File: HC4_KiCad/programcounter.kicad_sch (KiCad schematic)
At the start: 20 parts, among them IC13 74HC161, IC14 74HC161, IC15 74HC161

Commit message: フットプリントをSOPに変更
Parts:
- CP12, CP13, CP14: footprint Capacitor_THT:C_Disc_D3.0mm_W1.6mm_P2.50mm -> Capacitor_SMD:C_0603_1608Metric
- IC13, IC14, IC15: footprint Package_DIP:DIP-16_W7.62mm_Socket -> Package_SO:SO-16_5.3x10.2mm_P1.27mm
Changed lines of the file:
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@@
 			)
 		)
-		(property "Footprint" "Package_DIP:DIP-16_W7.62mm_Socket"
+		(property "Footprint" "Package_SO:SO-16_5.3x10.2mm_P1.27mm"
 			(at 127 33.02 0)
 			(effects
@@
 			)
 		)
-		(property "Footprint" "Capacitor_THT:C_Disc_D3.0mm_W1.6mm_P2.50mm"
+		(property "Footprint" "Capacitor_SMD:C_0603_1608Metric"
 			(at 125.4252 182.88 0)
 			(effects
@@
 			)
 		)
-		(property "Footprint" "Capacitor_THT:C_Disc_D3.0mm_W1.6mm_P2.50mm"
+		(property "Footprint" "Capacitor_SMD:C_0603_1608Metric"
 			(at 131.7752 182.88 0)
 			(effects
@@
 			)
 		)
-		(property "Footprint" "Package_DIP:DIP-16_W7.62mm_Socket"
+		(property "Footprint" "Package_SO:SO-16_5.3x10.2mm_P1.27mm"
 			(at 127 76.2 0)
 			(effects
@@
 			)
 		)
-		(property "Footprint" "Package_DIP:DIP-16_W7.62mm_Socket"
+		(property "Footprint" "Package_SO:SO-16_5.3x10.2mm_P1.27mm"
 			(at 127 120.65 0)
 			(effects
@@
 			)
 		)
-		(property "Footprint" "Capacitor_THT:C_Disc_D3.0mm_W1.6mm_P2.50mm"
+		(property "Footprint" "Capacitor_SMD:C_0603_1608Metric"
 			(at 119.0752 182.88 0)
 			(effects

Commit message: 基板ぬ
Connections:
- net at LD30.1 (K): now also RN5.2 (R1.2); no longer RN5.5 (R4.2)
- net at RN5.3 (R2.2): now also LD27.1 (K); no longer LD24.1 (K)
- net at LD29.1 (K): now also RN4.6 (R5.2); no longer RN4.9 (R8.2)
- net at RN5.4 (R3.2): now also LD24.1 (K); no longer LD27.1 (K)
- net at RN5.7 (R6.2): now also LD28.1 (K); no longer LD25.1 (K)
- net at LD20.1 (K): now also RN4.9 (R8.2); no longer RN4.6 (R5.2)
- net at RN5.8 (R7.2): now also LD25.1 (K); no longer LD28.1 (K)
- net at LD21.1 (K): now also RN5.5 (R4.2); no longer RN5.2 (R1.2)
- net at RN5.9 (R8.2): now also LD22.1 (K); no longer LD31.1 (K)
- net at LD23.1 (K): now also RN4.8 (R7.2); no longer RN4.7 (R6.2)
- net at RN5.6 (R5.2): now also LD31.1 (K); no longer LD22.1 (K)
- net at LD26.1 (K): now also RN4.7 (R6.2); no longer RN4.8 (R7.2)
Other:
- moved on the sheet: RN4E, RN4F, RN4G, RN4H, RN5A, RN5B, RN5C, RN5D, RN5E, RN5F, RN5G, RN5H

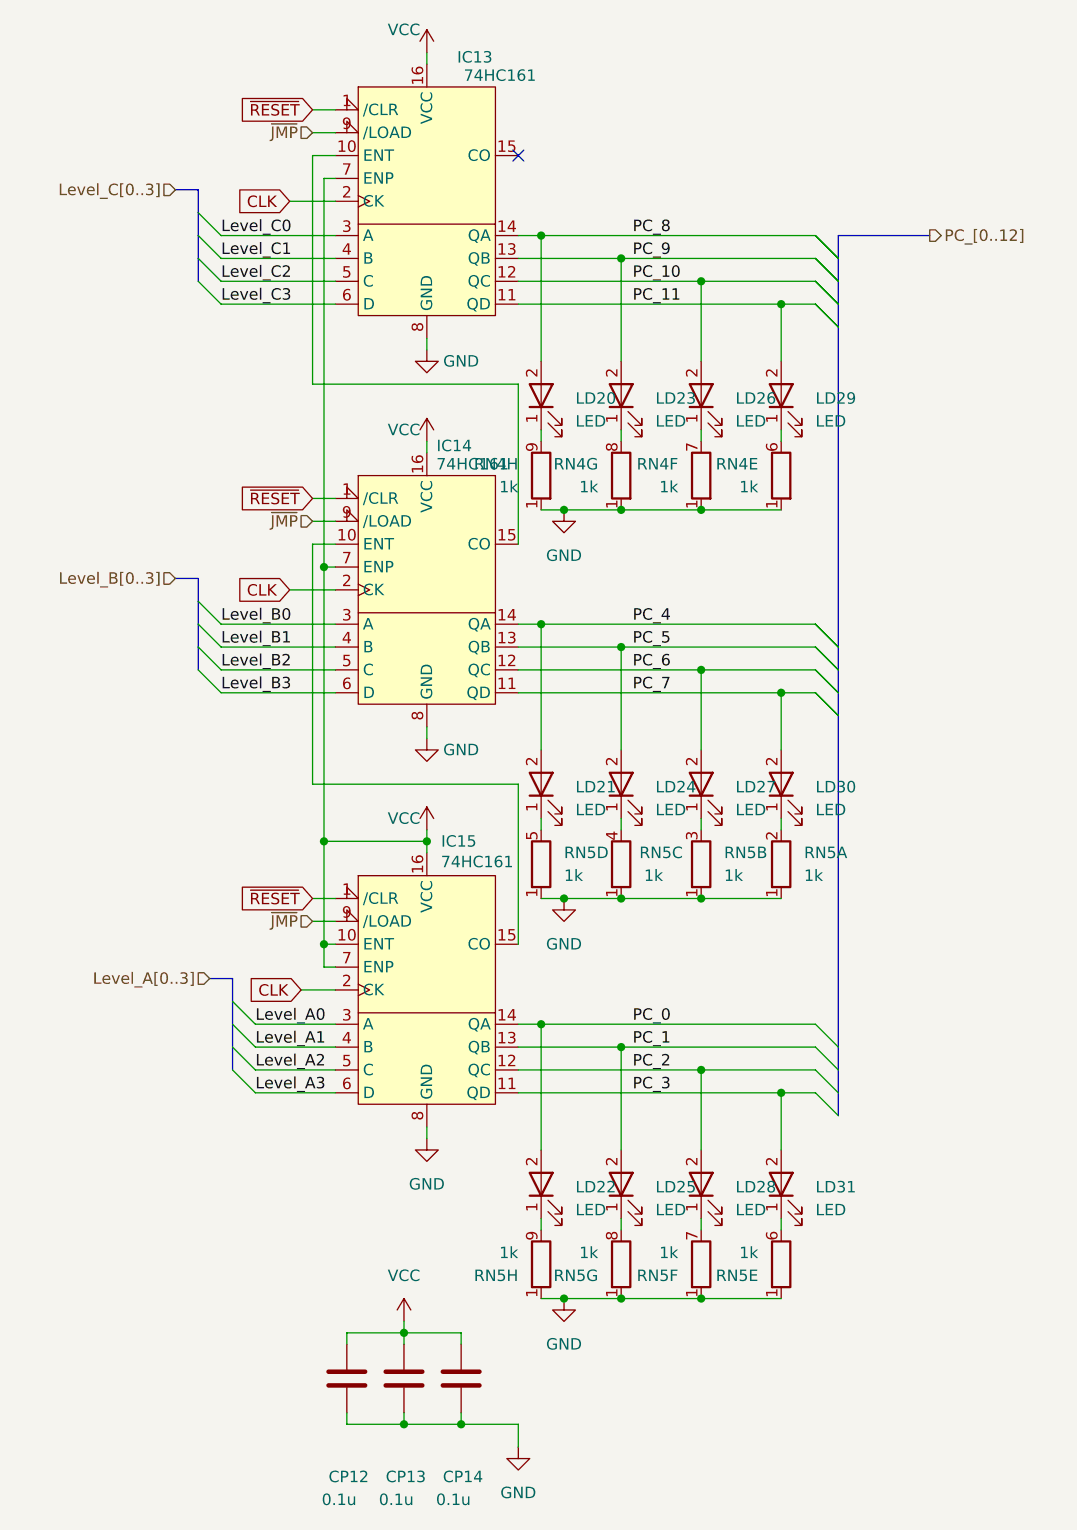
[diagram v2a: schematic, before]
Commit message: Added output port for blink
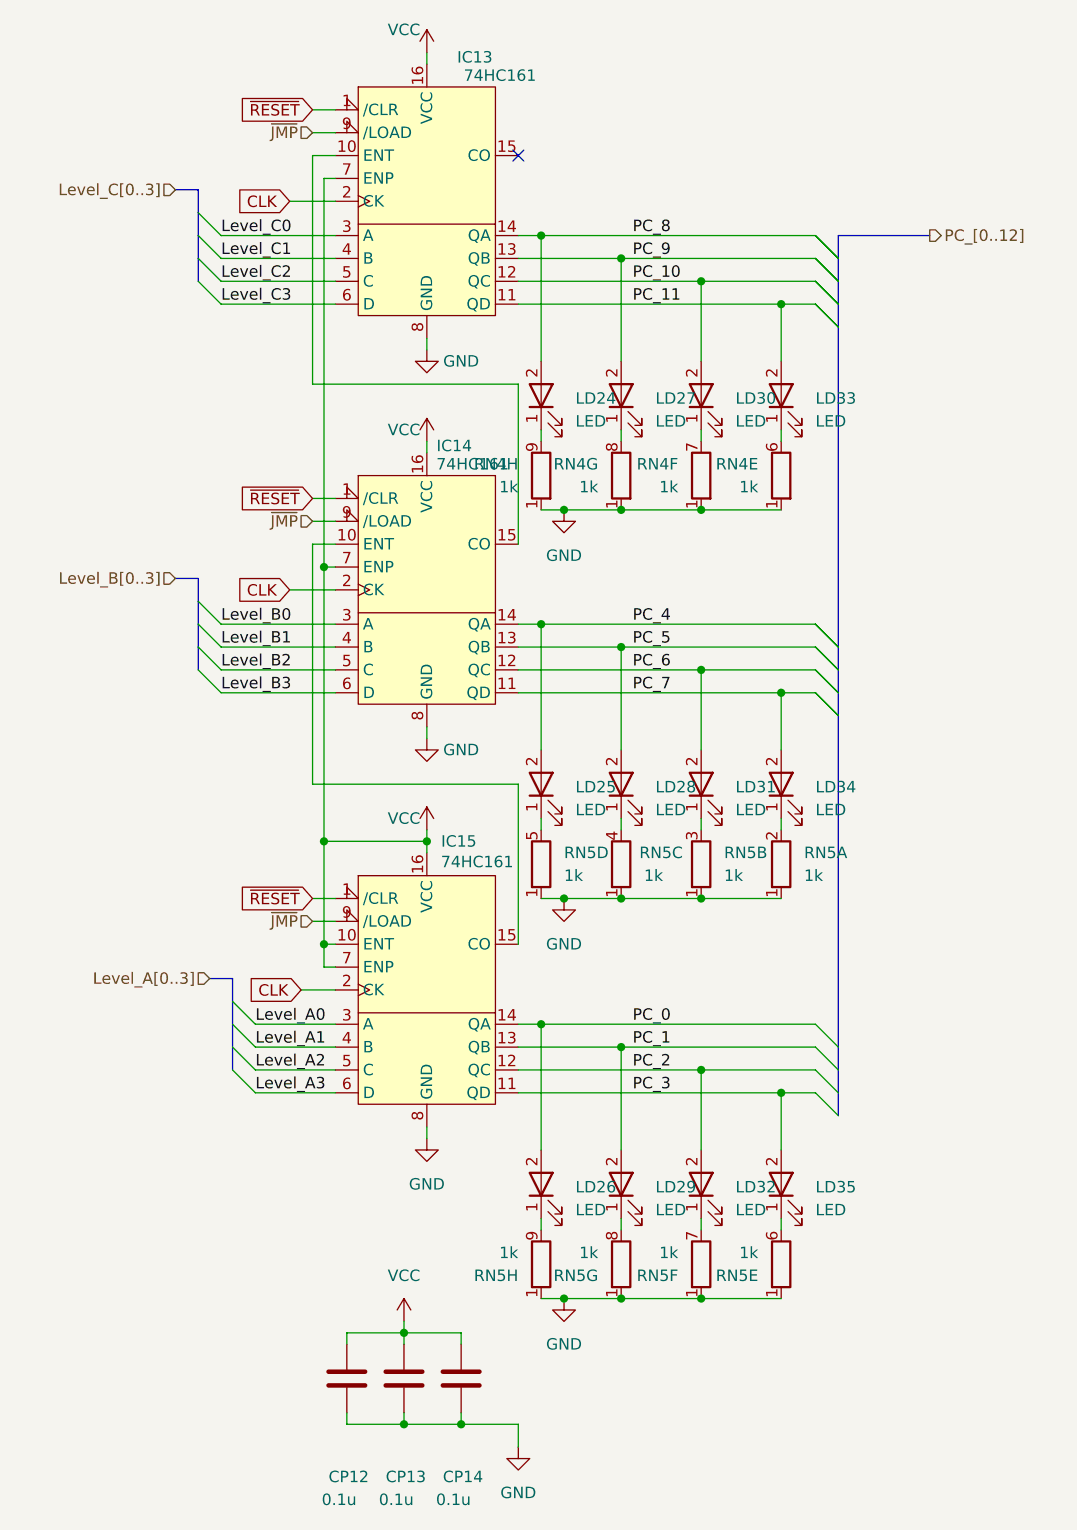
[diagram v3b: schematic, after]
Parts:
- renumbered LD20 to LD24, LD21 to LD25, LD22 to LD26, LD23 to LD27, LD24 to LD28, LD25 to LD29, LD26 to LD30, LD27 to LD31, LD28 to LD32, LD29 to LD33, LD30 to LD34, LD31 to LD35
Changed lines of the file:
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@@
 		(on_board yes)
 		(dnp no)
-		(property "Reference" "#PWR047"
+		(property "Reference" "#PWR046"
 			(at 127 114.3 0)
 			(effects
@@
 			(project "HC4_KiCad"
 				(path "/33731ded-38c0-4297-bdd8-92b082f46ff8/7ee18210-5407-4798-af07-3cd6c855784b"
-					(reference "#PWR047")
+					(reference "#PWR046")
 					(unit 1)
 				)
@@
 		(dnp no)
 		(fields_autoplaced yes)
-		(property "Reference" "LD30"
+		(property "Reference" "LD34"
 			(at 170.18 113.3474 90)
 			(effects
@@
 			)
 		)
-		(property "Datasheet" "~"
+		(property "Datasheet" ""
 			(at 166.37 113.03 0)
 			(effects
@@
 			(project "HC4_KiCad"
 				(path "/33731ded-38c0-4297-bdd8-92b082f46ff8/7ee18210-5407-4798-af07-3cd6c855784b"
-					(reference "LD30")
+					(reference "LD34")
 					(unit 1)
 				)
@@
 		(dnp no)
 		(fields_autoplaced yes)
-		(property "Reference" "#PWR053"
+		(property "Reference" "#PWR052"
 			(at 142.24 176.53 0)
 			(effects
@@
 			(project ""
 				(path "/33731ded-38c0-4297-bdd8-92b082f46ff8/7ee18210-5407-4798-af07-3cd6c855784b"
-					(reference "#PWR053")
+					(reference "#PWR052")
 					(unit 1)
 				)
@@
 		(dnp no)
 		(fields_autoplaced yes)
-		(property "Reference" "LD29"
+		(property "Reference" "LD33"
 			(at 170.18 70.1674 90)
 			(effects
@@
 			)
 		)
-		(property "Datasheet" "~"
+		(property "Datasheet" ""
 			(at 166.37 69.85 0)
 			(effects
@@
 			(project "HC4_KiCad"
 				(path "/33731ded-38c0-4297-bdd8-92b082f46ff8/7ee18210-5407-4798-af07-3cd6c855784b"
-					(reference "LD29")
+					(reference "LD33")
 					(unit 1)
 				)
@@
 		(dnp no)
 		(fields_autoplaced yes)
-		(property "Reference" "LD24"
+		(property "Reference" "LD28"
 			(at 152.4 113.3474 90)
 			(effects
@@
 			)
 		)
-		(property "Datasheet" "~"
+		(property "Datasheet" ""
 			(at 148.59 113.03 0)
 			(effects
@@
 			(project "HC4_KiCad"
 				(path "/33731ded-38c0-4297-bdd8-92b082f46ff8/7ee18210-5407-4798-af07-3cd6c855784b"
-					(reference "LD24")
+					(reference "LD28")
 					(unit 1)
 				)
@@
 		(on_board yes)
 		(dnp no)
-		(property "Reference" "#PWR045"
+		(property "Reference" "#PWR044"
 			(at 127 71.12 0)
 			(effects
@@
 			(project "HC4_KiCad"
 				(path "/33731ded-38c0-4297-bdd8-92b082f46ff8/7ee18210-5407-4798-af07-3cd6c855784b"
-					(reference "#PWR045")
+					(reference "#PWR044")
 					(unit 1)
 				)
@@
 		(on_board yes)
 		(dnp no)
-		(property "Reference" "#PWR046"
+		(property "Reference" "#PWR045"
 			(at 127 78.74 0)
 			(effects
@@
 			(project "HC4_KiCad"
 				(path "/33731ded-38c0-4297-bdd8-92b082f46ff8/7ee18210-5407-4798-af07-3cd6c855784b"
-					(reference "#PWR046")
+					(reference "#PWR045")
 					(unit 1)
 				)
@@
 		(dnp no)
 		(fields_autoplaced yes)
-		(property "Reference" "LD27"
+		(property "Reference" "LD31"
 			(at 161.29 113.3474 90)
 			(effects
@@
 			)
 		)
-		(property "Datasheet" "~"
+		(property "Datasheet" ""
 			(at 157.48 113.03 0)
 			(effects
@@
 			(project "HC4_KiCad"
 				(path "/33731ded-38c0-4297-bdd8-92b082f46ff8/7ee18210-5407-4798-af07-3cd6c855784b"
-					(reference "LD27")
+					(reference "LD31")
 					(unit 1)
 				)
@@
 		(on_board yes)
 		(dnp no)
-		(property "Reference" "#PWR048"
+		(property "Reference" "#PWR047"
 			(at 127 121.92 0)
 			(effects
@@
 			(project "HC4_KiCad"
 				(path "/33731ded-38c0-4297-bdd8-92b082f46ff8/7ee18210-5407-4798-af07-3cd6c855784b"
-					(reference "#PWR048")
+					(reference "#PWR047")
 					(unit 1)
 				)
@@
 		(dnp no)
 		(fields_autoplaced yes)
-		(property "Reference" "LD21"
+		(property "Reference" "LD25"
 			(at 143.51 113.3474 90)
 			(effects
@@
 			)
 		)
-		(property "Datasheet" "~"
+		(property "Datasheet" ""
 			(at 139.7 113.03 0)
 			(effects
@@
 			(project "HC4_KiCad"
 				(path "/33731ded-38c0-4297-bdd8-92b082f46ff8/7ee18210-5407-4798-af07-3cd6c855784b"
-					(reference "LD21")
+					(reference "LD25")
 					(unit 1)
 				)
@@
 		(dnp no)
 		(fields_autoplaced yes)
-		(property "Reference" "LD20"
+		(property "Reference" "LD24"
 			(at 143.51 70.1674 90)
 			(effects
@@
 			)
 		)
-		(property "Datasheet" "~"
+		(property "Datasheet" ""
 			(at 139.7 69.85 0)
 			(effects
@@
 			(project "HC4_KiCad"
 				(path "/33731ded-38c0-4297-bdd8-92b082f46ff8/7ee18210-5407-4798-af07-3cd6c855784b"
-					(reference "LD20")
+					(reference "LD24")
 					(unit 1)
 				)
@@
 		(dnp no)
 		(fields_autoplaced yes)
-		(property "Reference" "#PWR052"
+		(property "Reference" "#PWR051"
 			(at 142.24 132.08 0)
 			(effects
@@
 			(project ""
 				(path "/33731ded-38c0-4297-bdd8-92b082f46ff8/7ee18210-5407-4798-af07-3cd6c855784b"
-					(reference "#PWR052")
+					(reference "#PWR051")
 					(unit 1)
 				)
@@
 		(dnp no)
 		(fields_autoplaced yes)
-		(property "Reference" "LD23"
+		(property "Reference" "LD27"
 			(at 152.4 70.1674 90)
 			(effects
@@
 			)
 		)
-		(property "Datasheet" "~"
+		(property "Datasheet" ""
 			(at 148.59 69.85 0)
 			(effects
@@
 			(project "HC4_KiCad"
 				(path "/33731ded-38c0-4297-bdd8-92b082f46ff8/7ee18210-5407-4798-af07-3cd6c855784b"
-					(reference "LD23")
+					(reference "LD27")
 					(unit 1)
 				)
@@
 		(dnp no)
 		(fields_autoplaced yes)
-		(property "Reference" "#PWR051"
+		(property "Reference" "#PWR050"
 			(at 142.24 88.9 0)
 			(effects
@@
 			(project ""
 				(path "/33731ded-38c0-4297-bdd8-92b082f46ff8/7ee18210-5407-4798-af07-3cd6c855784b"
-					(reference "#PWR051")
+					(reference "#PWR050")
 					(unit 1)
 				)
@@
 		(dnp no)
 		(fields_autoplaced yes)
-		(property "Reference" "#PWR049"
+		(property "Reference" "#PWR048"
 			(at 127 158.75 0)
 			(effects
@@
 			(project "HC4_KiCad"
 				(path "/33731ded-38c0-4297-bdd8-92b082f46ff8/7ee18210-5407-4798-af07-3cd6c855784b"
-					(reference "#PWR049")
+					(reference "#PWR048")
 					(unit 1)
 				)
@@
 		(dnp no)
 		(fields_autoplaced yes)
-		(property "Reference" "#PWR043"
+		(property "Reference" "#PWR042"
 			(at 124.46 176.53 0)
 			(effects
@@
 			(project ""
 				(path "/33731ded-38c0-4297-bdd8-92b082f46ff8/7ee18210-5407-4798-af07-3cd6c855784b"
-					(reference "#PWR043")
+					(reference "#PWR042")
 					(unit 1)
 				)
@@
 		(dnp no)
 		(fields_autoplaced yes)
-		(property "Reference" "LD28"
+		(property "Reference" "LD32"
 			(at 161.29 157.7974 90)
 			(effects
@@
 			)
 		)
-		(property "Datasheet" "~"
+		(property "Datasheet" ""
 			(at 157.48 157.48 0)
 			(effects
@@
 			(project "HC4_KiCad"
 				(path "/33731ded-38c0-4297-bdd8-92b082f46ff8/7ee18210-5407-4798-af07-3cd6c855784b"
-					(reference "LD28")
+					(reference "LD32")
 					(unit 1)
 				)
@@
 		(dnp no)
 		(fields_autoplaced yes)
-		(property "Reference" "LD22"
+		(property "Reference" "LD26"
 			(at 143.51 157.7974 90)
 			(effects
@@
 			)
 		)
-		(property "Datasheet" "~"
+		(property "Datasheet" ""
 			(at 139.7 157.48 0)
 			(effects
@@
 			(project "HC4_KiCad"
 				(path "/33731ded-38c0-4297-bdd8-92b082f46ff8/7ee18210-5407-4798-af07-3cd6c855784b"
-					(reference "LD22")
+					(reference "LD26")
 					(unit 1)
 				)
@@
 		(dnp no)
 		(fields_autoplaced yes)
-		(property "Reference" "LD31"
+		(property "Reference" "LD35"
 			(at 170.18 157.7974 90)
 			(effects
@@
 			)
 		)
-		(property "Datasheet" "~"
+		(property "Datasheet" ""
 			(at 166.37 157.48 0)
 			(effects
@@
 			(project "HC4_KiCad"
 				(path "/33731ded-38c0-4297-bdd8-92b082f46ff8/7ee18210-5407-4798-af07-3cd6c855784b"
-					(reference "LD31")
+					(reference "LD35")
 					(unit 1)
 				)
@@
 		(dnp no)
 		(fields_autoplaced yes)
-		(property "Reference" "#PWR050"
+		(property "Reference" "#PWR049"
 			(at 137.16 193.04 0)
 			(effects
@@
 			(project ""
 				(path "/33731ded-38c0-4297-bdd8-92b082f46ff8/7ee18210-5407-4798-af07-3cd6c855784b"
-					(reference "#PWR050")
+					(reference "#PWR049")
 					(unit 1)
 				)
@@
 		(dnp no)
 		(fields_autoplaced yes)
-		(property "Reference" "LD26"
+		(property "Reference" "LD30"
 			(at 161.29 70.1674 90)
 			(effects
@@
 			)
 		)
-		(property "Datasheet" "~"
+		(property "Datasheet" ""
 			(at 157.48 69.85 0)
 			(effects
@@
 			(project "HC4_KiCad"
 				(path "/33731ded-38c0-4297-bdd8-92b082f46ff8/7ee18210-5407-4798-af07-3cd6c855784b"
-					(reference "LD26")
+					(reference "LD30")
 					(unit 1)
 				)
@@
 		(dnp no)
 		(fields_autoplaced yes)
-		(property "Reference" "LD25"
+		(property "Reference" "LD29"
 			(at 152.4 157.7974 90)
 			(effects
@@
 			)
 		)
-		(property "Datasheet" "~"
+		(property "Datasheet" ""
 			(at 148.59 157.48 0)
 			(effects
@@
 			(project "HC4_KiCad"
 				(path "/33731ded-38c0-4297-bdd8-92b082f46ff8/7ee18210-5407-4798-af07-3cd6c855784b"
-					(reference "LD25")
+					(reference "LD29")
 					(unit 1)
 				)
@@
 		(on_board yes)
 		(dnp no)
-		(property "Reference" "#PWR044"
+		(property "Reference" "#PWR043"
 			(at 127 35.56 0)
 			(effects
@@
 			(project "HC4_KiCad"
 				(path "/33731ded-38c0-4297-bdd8-92b082f46ff8/7ee18210-5407-4798-af07-3cd6c855784b"
-					(reference "#PWR044")
+					(reference "#PWR043")
 					(unit 1)
 				)
